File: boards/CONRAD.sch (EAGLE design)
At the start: 59 parts, among them Q1 2N7002L, Q2 DMP3099L, U1 TXB0104, U2 RMX-GNSS-TM, U3 CD74HC137D, U4 BME280, U5 BMX055, U6 DS3231MZ+SOIC8, U7 LMC555D, U8 CAT24C256WI-GT3, U9 LMZ21700, X1 SMA-142-0711-821/826

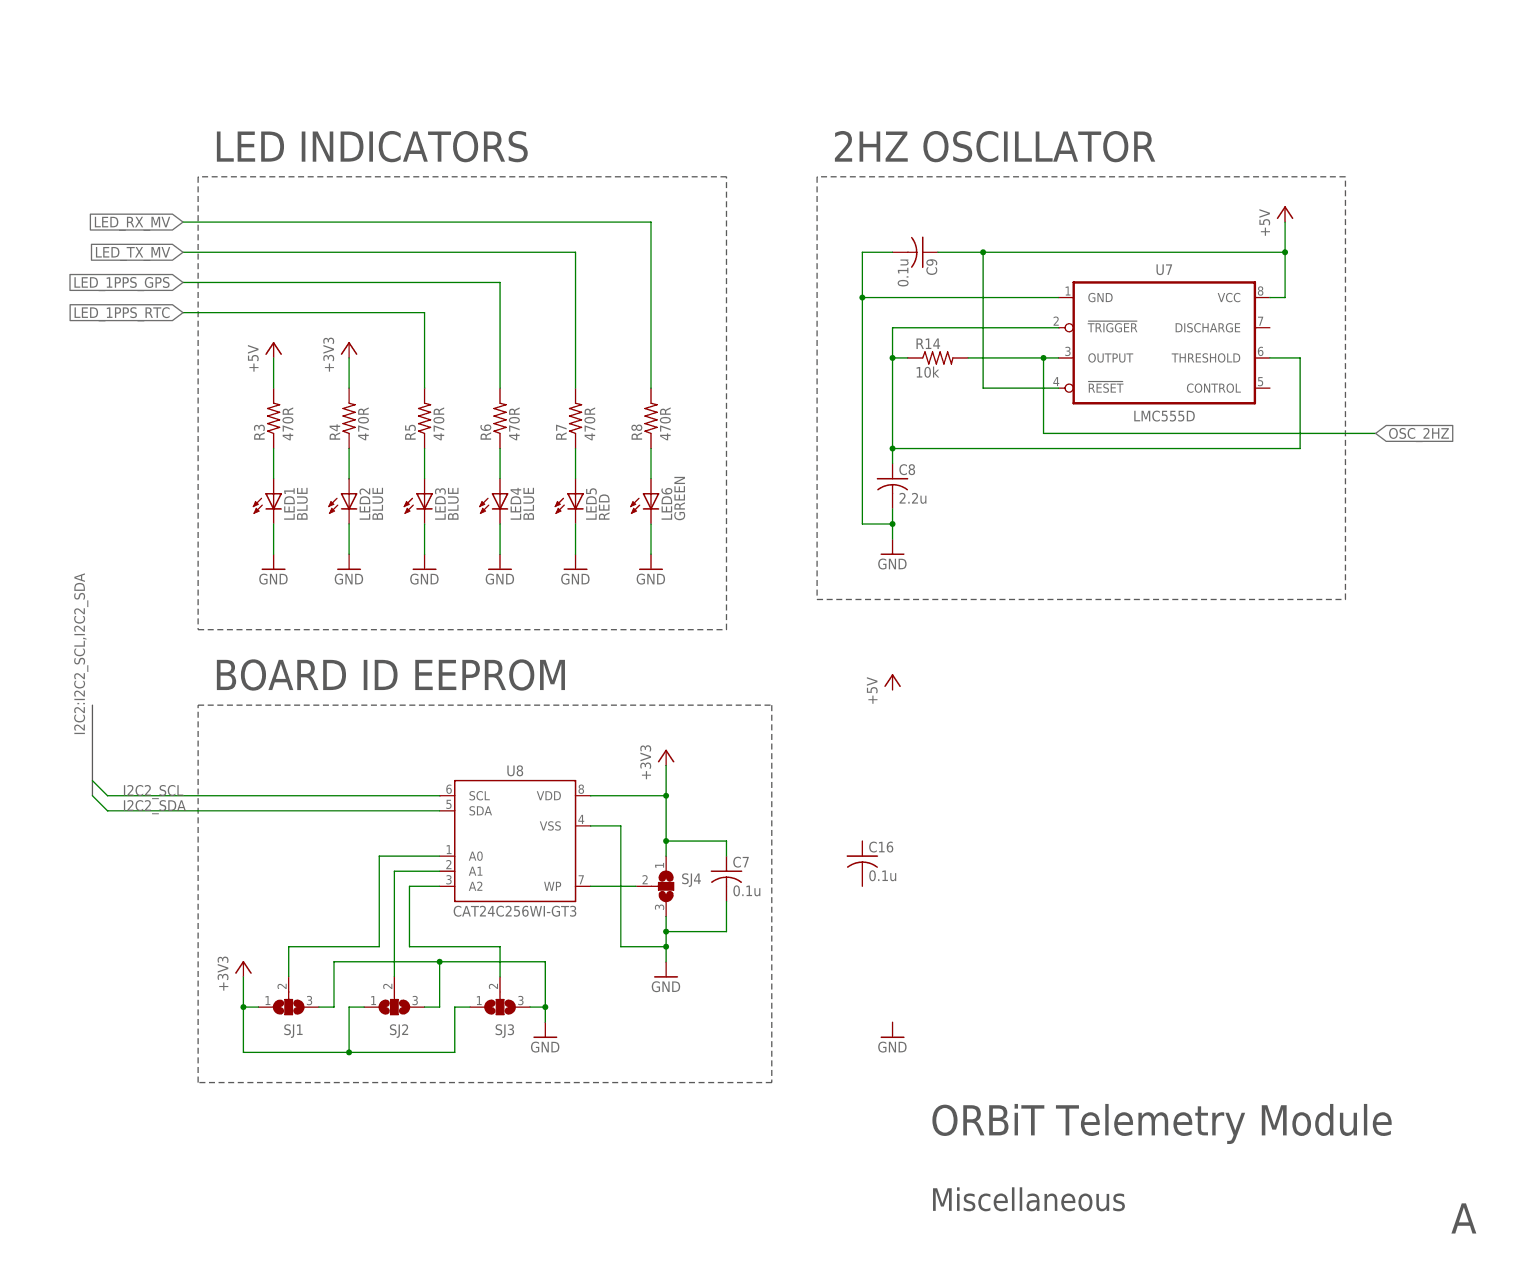
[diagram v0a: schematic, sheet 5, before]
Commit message: Finished basic functionality for telemetry board
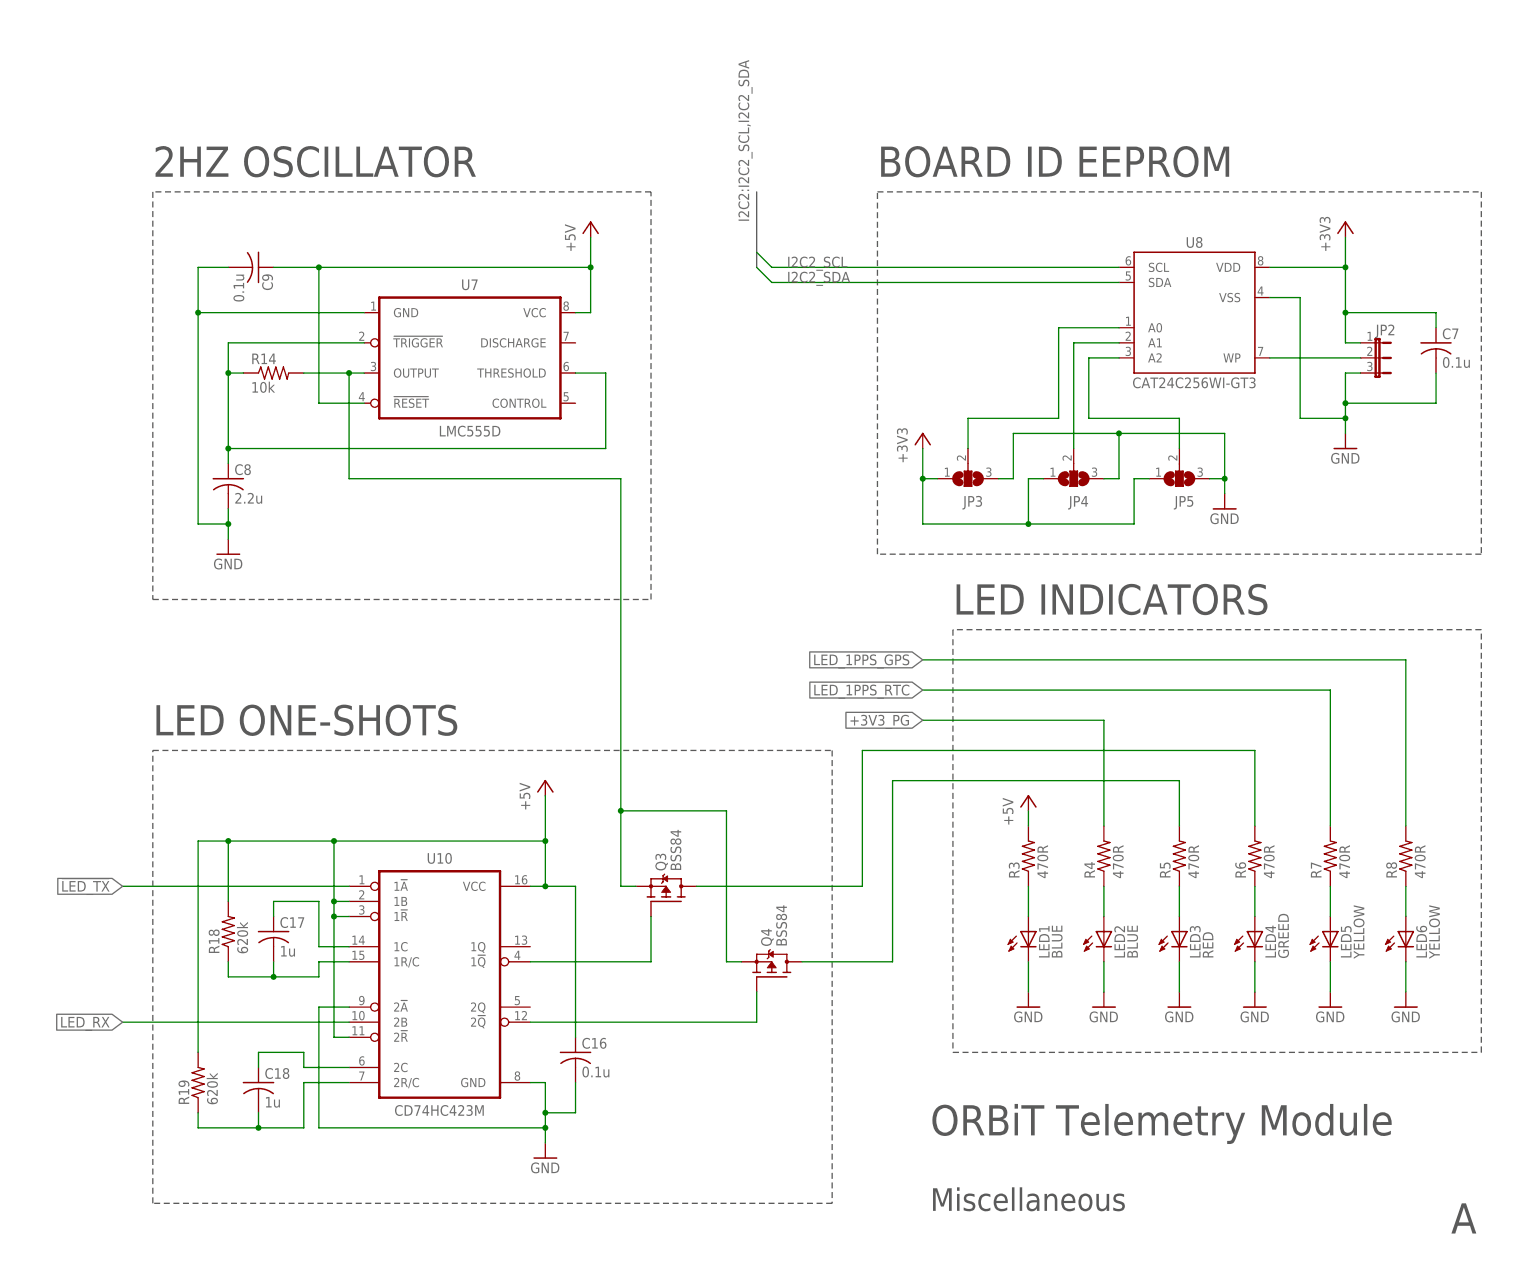
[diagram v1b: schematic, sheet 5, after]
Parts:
- removed SJ1, SJ2, SJ3, SJ4: (no value), jumper:SJ2W
- added C17, C18: 1u, rcl:C-USC0805
- added C19: 0.1u, rcl:C-USC0805
- added JP1, JP2: (no value), jumper:JP2E
- added JP3, JP4, JP5: (no value), jumper:SJ2W
- added Q3, Q4: BSS84, ORBiT-transistors:PMOSSOT23-3
- added R18, R19: 620k, rcl:R-US_R0805
- added U10: CD74HC423M, ORBiT-IC-TI:CD74HC423M
- added X2: (no value), ORBiT-con-Molex-Nano-Fit:105314-06
- C11: value 1u -> 22u
- LED3: value BLUE -> RED
- LED4: value BLUE -> GREED
- LED5: value RED -> YELLOW
- LED6: value GREEN -> YELLOW
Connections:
- removed net LED_TX: PCB2.!TX_PWR!
- new net !LED_TX: PCB2.!TX_PWR!, U10.1!A
- new net +3V3_PG: R15.1, R4.2, U9.PG
- new net N$29: C17.1, U10.1C
- new net N$30: C18.2, R19.1, U10.2R/C
- new net N$31: C18.1, U10.2C
- new net N$32: Q4.G, U10.2!Q
- new net N$33: Q3.G, U10.1!Q
- new net N$34: B1.+, C10.1, C11.1, JP1.3
- net +3V3: now also C1.1, C2.1, JP1.1, JP2.1, JP3.1, JP4.1, JP5.1, U3.G1, X2.2; no longer C1.2, C2.2, R4.2, SJ1.1, SJ2.1, SJ3.1, SJ4.1
- net +5V: now also C16.1, R18.2, R19.2, U10.1!R, U10.1B, U10.2!R, U10.VCC
- net GND: now also C1.2, C16.2, C19.2, C2.2, JP2.3, JP3.3, JP4.3, JP5.3, U10.2!A, U10.GND, X2.1; no longer C1.1, C2.1, SJ1.3, SJ2.3, SJ3.3, SJ4.3
- net LED_1PPS_GPS: now also R8.2; no longer R6.2
- net LED_1PPS_RTC: now also R7.2; no longer R5.2
- net LED_RX: now also U10.2B
- net LED_RX_MV: now also Q3.D, R6.2; no longer R8.2
- net LED_TX_MV: now also Q4.D, R5.2; no longer R7.2
- net N$20: now also JP3.2; no longer SJ1.2
- net N$21: now also JP4.2; no longer SJ2.2
- net N$22: now also JP5.2; no longer SJ3.2
- net N$23: now also JP2.2; no longer SJ4.2
- net N$27: now also C17.2, R18.1, U10.1R/C; no longer R15.1, U9.PG
- net N$9: now also U3.Y4, X2.3; no longer U3.G1
- net OSC_2HZ: now also Q3.S, Q4.S
- net SPI0_CLK: now also X2.4
- net SPI0_MISO: now also X2.6
- net SPI0_MOSI: now also X2.5
- net VBAT: now also C19.1, JP1.2; no longer B1.+, C10.1, C11.1
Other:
- note added: "EXTERNAL IMU"
- note added: "LED ONE-SHOTS"
- note added: "ONBOARD IMU"
- note added: "Radios and RTC"
- note removed: "9-AXIS IMU"
- note removed: "Radios"
- moved on the sheet: B1, C1, C10, C11, C16, C2, C3, C7, C8, C9, L1, LED1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

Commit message: CONRAD - Added test points
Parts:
- added TP1, TP10, TP11, TP12, TP13, TP14, TP15, TP16, TP17, TP18, TP19, TP2, TP20, TP21, TP22, TP23, TP24, TP25, TP26, TP27, TP28, TP29, TP3, TP30, TP31, TP32, TP33, TP4, TP5, TP6, TP7, TP8, TP9: TP063, ORBiT-special:TP063
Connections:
- net +3V3: now also TP4.TP
- net +3V3_PG: now also TP11.TP
- net +5V: now also TP3.TP
- net +5V_BBB: now also TP1.TP
- net I2C1_SCL: now also TP12.TP
- net I2C1_SDA: now also TP13.TP
- net I2C2_SCL: now also TP14.TP
- net I2C2_SDA: now also TP15.TP
- net LED_1PPS_GPS: now also TP7.TP
- net LED_1PPS_RTC: now also TP8.TP
- net LED_RX_MV: now also TP9.TP
- net LED_TX_MV: now also TP10.TP
- net N$10: now also TP29.TP
- net N$11: now also TP31.TP
- net N$12: now also TP30.TP
- net N$13: now also TP32.TP
- net N$9: now also TP33.TP
- net OSC_2HZ: now also TP6.TP
- net SPI0_A0: now also TP22.TP
- net SPI0_A1: now also TP21.TP
- net SPI0_A2: now also TP20.TP
- net SPI0_CLK: now also TP19.TP
- net SPI0_CS: now also TP18.TP
- net SPI0_MISO: now also TP17.TP
- net SPI0_MOSI: now also TP16.TP
- net SYS_RESETN: now also TP2.TP
- net UART4_CTSN: now also TP23.TP
- net UART4_RTSN: now also TP24.TP
- net UART4_RXD: now also TP25.TP
- net UART4_TXD: now also TP26.TP
- net UART5_RXD: now also TP27.TP
- net UART5_TXD: now also TP28.TP
- net VBAT: now also TP5.TP
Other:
- note added: "+3V3"
- note added: "+5V"
- note added: "1-2 INTERNAL 3V3 REGULATOR 2-3 CR2032 BATTERY"
- note added: "1PPS_GPS"
- note added: "1PPS_RTC"
- note added: "ADDRESS SELECT"
- note added: "RX"
- note added: "TX"
- note added: "Z = 50Ω"
- moved on the sheet: B1, C1, C10, C11, C13, C14, C15, C16, C17, C18, C19, C2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
